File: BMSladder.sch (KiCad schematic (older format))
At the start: 30 parts, among them J1 Solder in Crimp, J2 Solder in Crimp, J3 HY2.0 Male, J4 Pad TH 1mm, J5 UPDI Port, J6 HY2.0 Male, J7 Solder in Crimp, Q1 MMDT3946, Q2 SI3402-TP, Q3 MMBT3904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

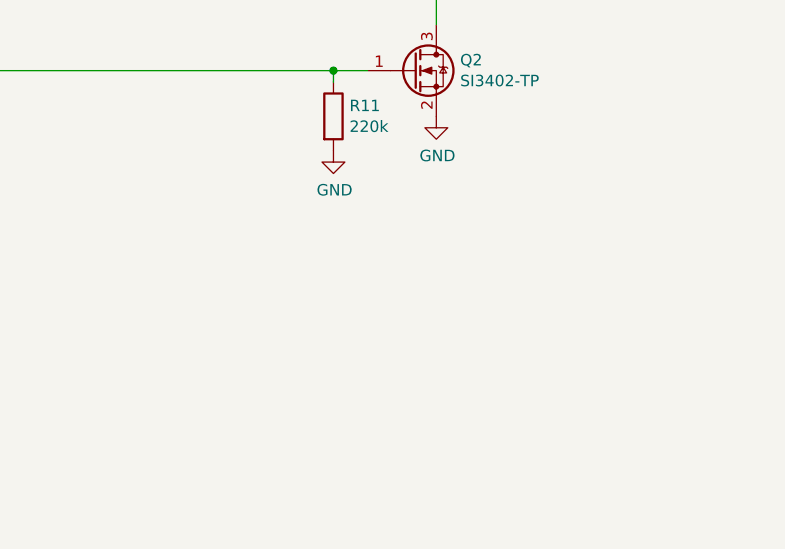
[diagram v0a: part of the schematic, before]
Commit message: Update BMSladder.sch
Added construction notes for further clarification
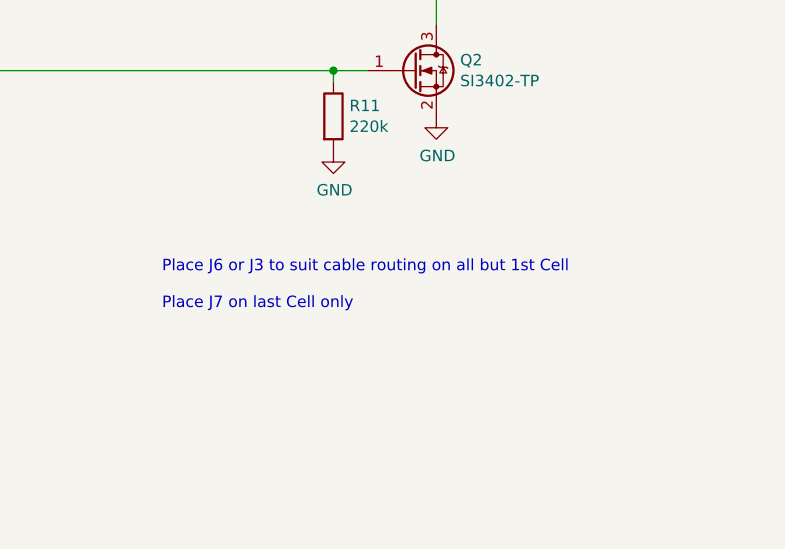
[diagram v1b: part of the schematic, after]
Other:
- note added: "Place J6 or J3 to suit cable routing on all but 1st Cell\n\nPlace J7 on last Cell only"
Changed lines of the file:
@@
 Wire Wire Line
 	5650 2800 6150 2800
+Text Notes 6900 5800 0    50   ~ 0
+Place J6 or J3 to suit cable routing on all but 1st Cell\n\nPlace J7 on last Cell only
 $EndSCHEMATC

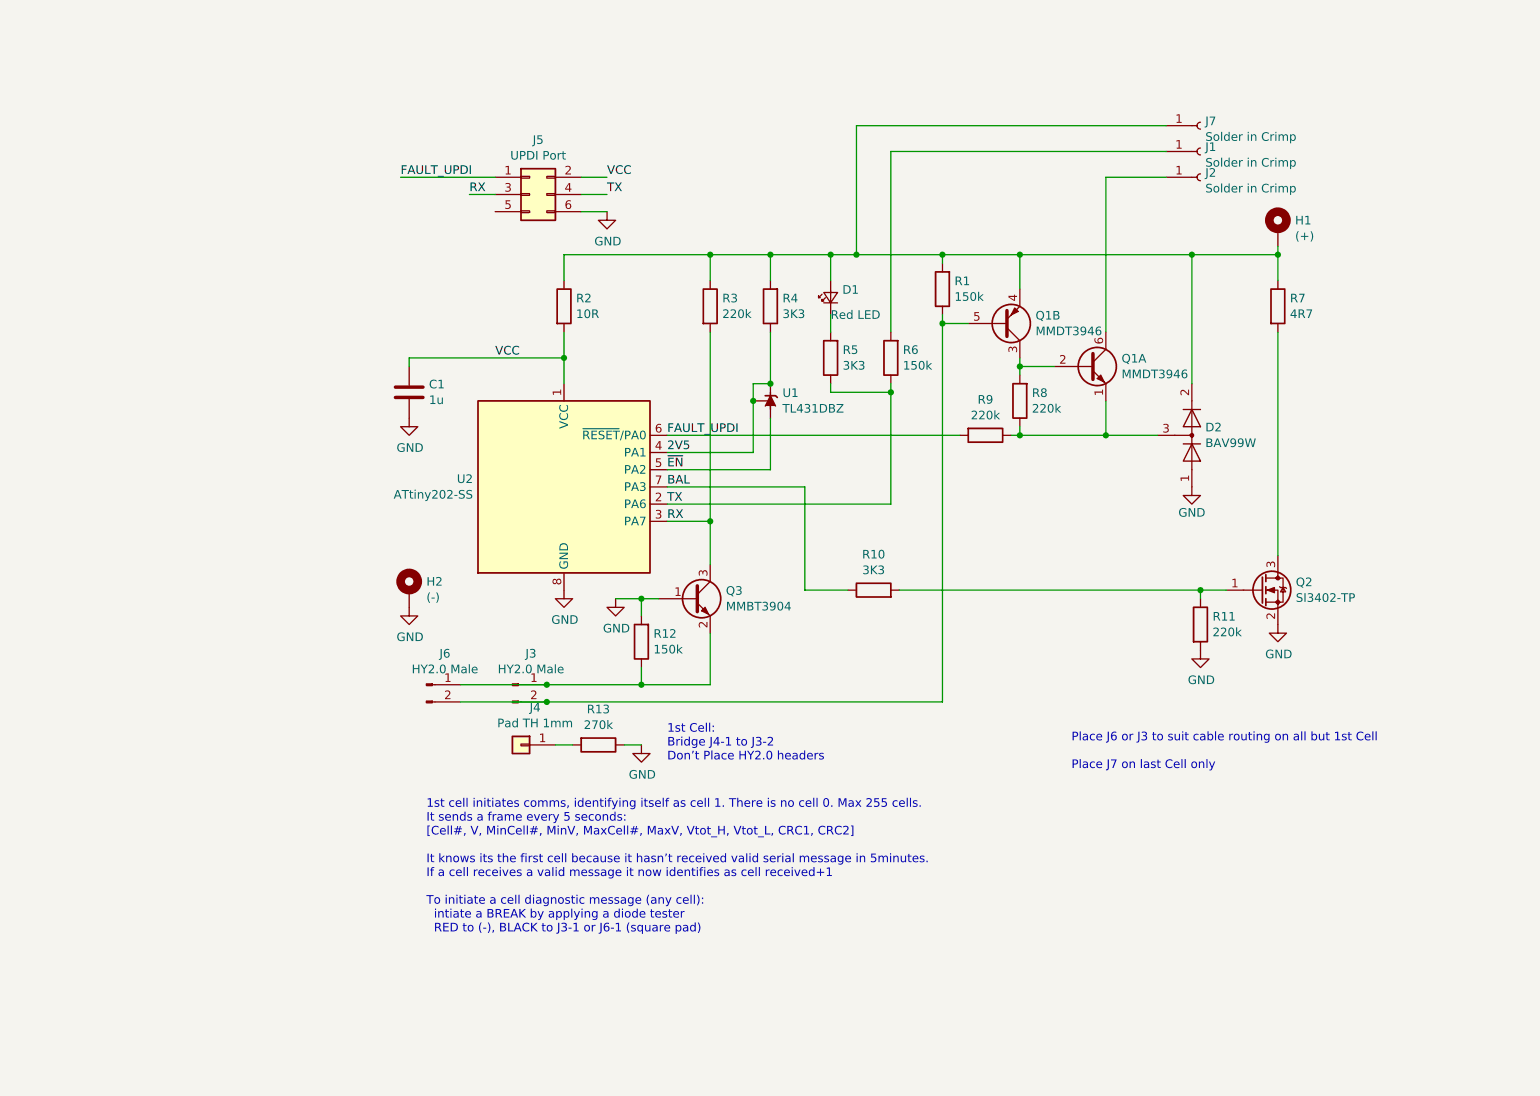
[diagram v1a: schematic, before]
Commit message: Improve connections
Most fiddly thing with v1.0 was the tail and connectors. changing to a surface mount connector (easy assembly), commonly available lead (if modified to remove one wire).
Also, uC pin swap as per Heins mod
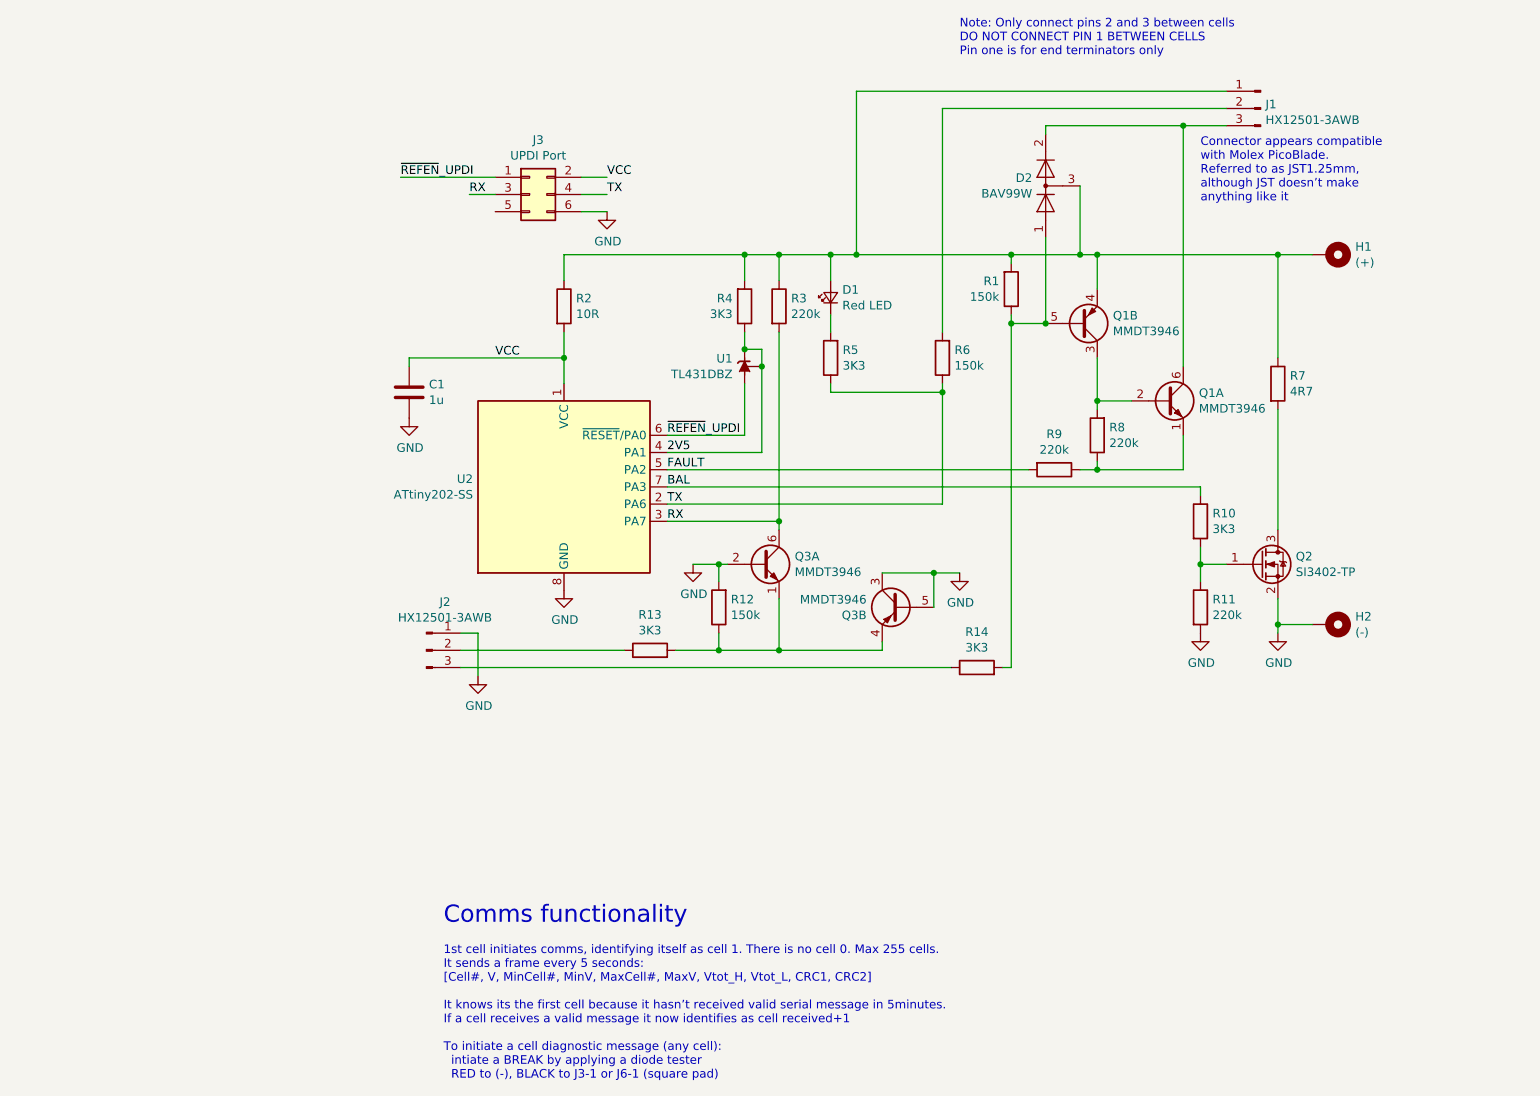
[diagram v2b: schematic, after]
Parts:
- removed J1, J2, J7: Solder in Crimp, Connector_Pin:Pin_D0.9mm_L10.0mm_W2.4mm_FlatFork, symbol Connector:Conn_01x01_Female
- removed J3, J6: HY2.0 Male, EdsKicadLibrary:HY2.0mm2P_Header_Horizontal, symbol Connector:Conn_01x02_Male
- removed J4: Pad TH 1mm, Connector_Pin:Pin_D1.0mm_L10.0mm, symbol Connector_Generic:Conn_01x01
- removed Q3: MMBT3904, Package_TO_SOT_SMD:SOT-23, symbol Transistor_BJT:MMBT3904
- added J1, J2: HX12501-3AWB, Connector_Molex:Molex_PicoBlade_53261-0371_1x03-1MP_P1.25mm_Horizontal, symbol Connector:Conn_01x03_Male
- added Q3: MMDT3946, Package_TO_SOT_SMD:SOT-363_SC-70-6, symbol Transistor_BJT:MMDT3946
- added R14: 3K3, Resistor_SMD:R_0603_1608Metric, symbol Device:R
- R13: value 270k -> 3K3
- renumbered J5 to J3
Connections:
- net GND: now also J2.1 (Pin_1), Q3.2 (B1), Q3.3 (C2), Q3.5 (B2); no longer D2.1 (K), R13.1
- net RX: now also Q3.6 (C1)
- net at R12.1: now also R13.2, Q3.1 (E1), Q3.4 (E2)
- net at Q1.1 (E1), R8.1, R9.1: no longer D2.3 (K)
- net at Q1.6 (C1): now also D2.2 (A), J1.3 (Pin_3)
- net at D1.2 (A), H1.1, Q1.4 (E2)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: now also D2.3 (K), J1.1 (Pin_1); no longer D2.2 (A)
- net at Q1.5 (B2), R1.1: now also D2.1 (K), R14.2
- net at R6.2: now also J1.2 (Pin_2)
- net FAULT_UPDI renamed ~REFEN~_UPDI
- net ~REFEN~_UPDI: now also U1.3 (A); no longer R9.2
- net ~EN renamed FAULT
- net FAULT: now also R9.2; no longer U1.3 (A)
- new net: J2.2 (Pin_2), R13.1
- new net: J2.3 (Pin_3), R14.1
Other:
- note added: "Comms functionality"
- note added: "Connector appears compatible\nwith Molex PicoBlade.\nReferred to as JST1.25mm,\nalthough JST doesn’t make\nanything like it"
- note added: "Note: Only connect pins 2 and 3 between cells\nDO NOT CONNECT PIN 1 BETWEEN CELLS\nPin one is for end terminators only"
- note removed: "1st Cell:\nBridge J4-1 to J3-2\nDon’t Place HY2.0 headers"
- note removed: "Place J6 or J3 to suit cable routing on all but 1st Cell\n\nPlace J7 on last Cell only"
- moved on the sheet: D2, H1, H2, Q1A, Q1B, Q2, R1, R10, R11, R12, R3, R4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

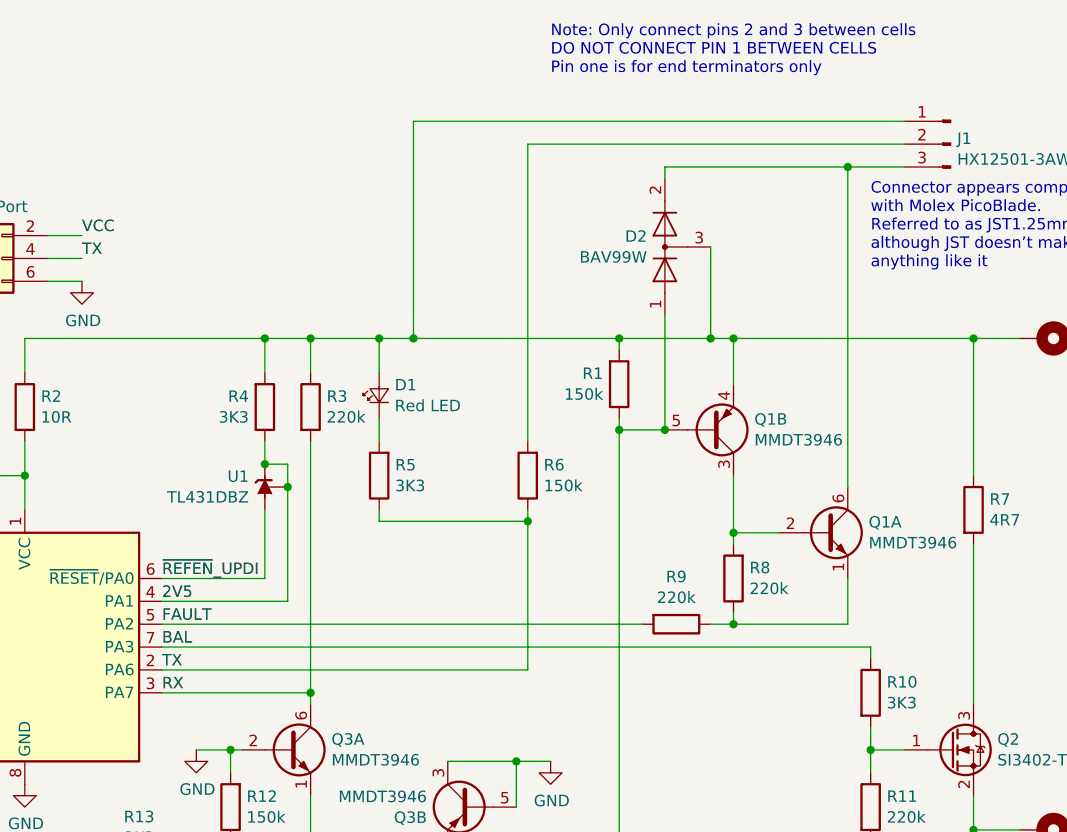
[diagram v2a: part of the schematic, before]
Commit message: old changes kept just in case
not sure why
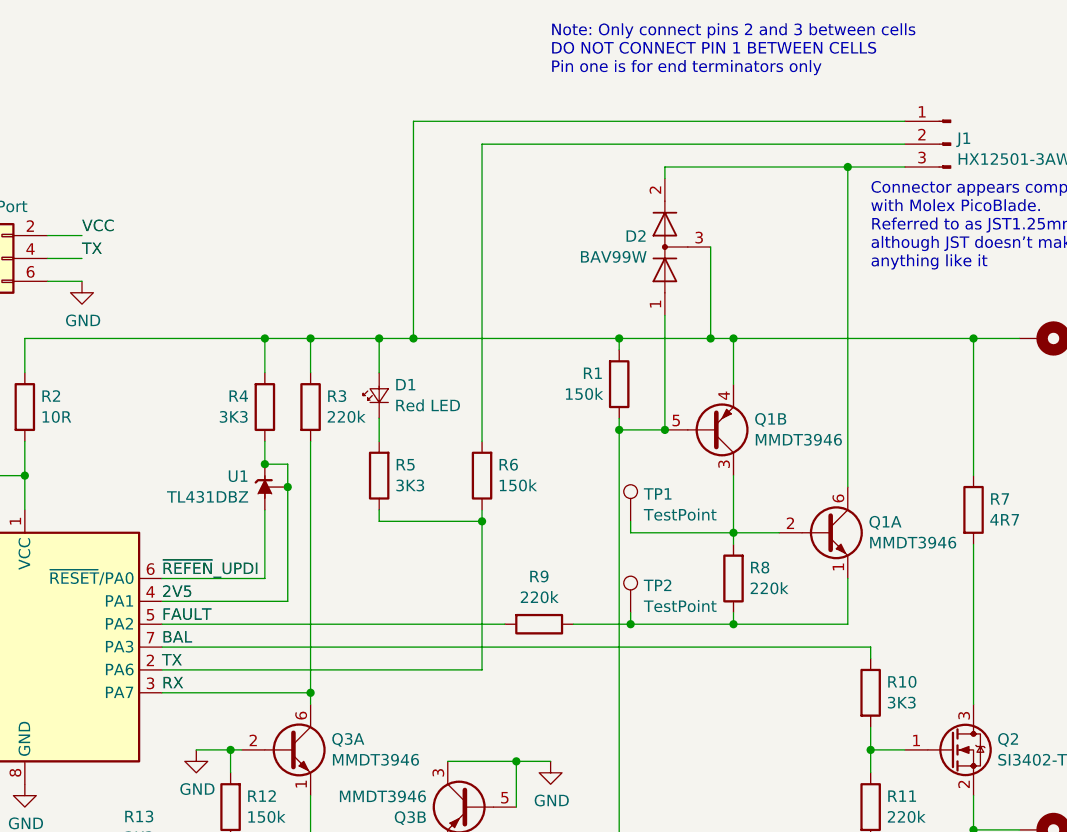
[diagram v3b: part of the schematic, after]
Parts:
- added TP1, TP2: TestPoint, TestPoint:TestPoint_Pad_D2.0mm, symbol Connector:TestPoint
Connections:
- net at Q1.1 (E1), R8.1, R9.1: now also TP2.1
- net at Q1.2 (B1), Q1.3 (C2), R8.2: now also TP1.1
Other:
- moved on the sheet: R6, R9
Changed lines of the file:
@@
 	3950 3250 3950 3400
 Wire Wire Line
-	6150 3250 6150 1950
+	5950 3250 5950 1950
 Wire Wire Line
 	5200 3250 5200 4350
@@
 	5500 3550 5500 3600
 Wire Wire Line
-	5500 3600 6150 3600
-Wire Wire Line
-	6150 3600 6150 3550
+	5500 3600 5950 3600
+Wire Wire Line
+	5950 3600 5950 3550
 Wire Wire Line
 	7050 4000 7050 4050
@@
 L Device:R R9
 U 1 1 619AAA79
-P 6800 4050
-F 0 "R9" V 6593 4050 50  0000 C CNN
-F 1 "220k" V 6684 4050 50  0000 C CNN
-F 2 "Resistor_SMD:R_0603_1608Metric" V 6730 4050 50  0001 C CNN
-F 3 "~" H 6800 4050 50  0001 C CNN
-	1    6800 4050
+P 6200 4050
+F 0 "R9" V 5993 4050 50  0000 C CNN
+F 1 "220k" V 6084 4050 50  0000 C CNN
+F 2 "Resistor_SMD:R_0603_1608Metric" V 6130 4050 50  0001 C CNN
+F 3 "~" H 6200 4050 50  0001 C CNN
+	1    6200 4050
 	0    1    1    0
 $EndComp
@@
 L Device:R R6
 U 1 1 619AB3DF
-P 6150 3400
-F 0 "R6" H 6080 3354 50  0000 R CNN
-F 1 "150k" H 6080 3445 50  0000 R CNN
-F 2 "Resistor_SMD:R_0603_1608Metric" V 6080 3400 50  0001 C CNN
-F 3 "~" H 6150 3400 50  0001 C CNN
-	1    6150 3400
+P 5950 3400
+F 0 "R6" H 5880 3354 50  0000 R CNN
+F 1 "150k" H 5880 3445 50  0000 R CNN
+F 2 "Resistor_SMD:R_0603_1608Metric" V 5880 3400 50  0001 C CNN
+F 3 "~" H 5950 3400 50  0001 C CNN
+	1    5950 3400
 	-1   0    0    1
 $EndComp
@@
 Connection ~ 8100 2800
 Wire Wire Line
-	6150 1950 7800 1950
+	5950 1950 7800 1950
 Wire Wire Line
 	7550 2050 7800 2050
@@
 Connection ~ 5000 2800
 Wire Wire Line
-	6150 4250 6150 3600
-Wire Wire Line
-	4550 4250 6150 4250
-Connection ~ 6150 3600
+	5950 4250 5950 3600
+Wire Wire Line
+	4550 4250 5950 4250
+Connection ~ 5950 3600
 Wire Wire Line
 	5500 2950 5500 2800
@@
 	5000 3850 4550 3850
 Wire Wire Line
-	6650 4050 4550 4050
-Wire Wire Line
-	7050 4050 6950 4050
+	6050 4050 4550 4050
+Wire Wire Line
+	7050 4050 6600 4050
 Connection ~ 7050 4050
 $Comp
@@
 Text Notes 7650 2500 0    50   ~ 0
 Connector appears compatible\nwith Molex PicoBlade.\nReferred to as JST1.25mm,\nalthough JST doesn’t make\nanything like it
+$Comp
+L Connector:TestPoint TP1
+U 1 1 6393EAFB
+P 6600 3600
+F 0 "TP1" H 6658 3718 50  0000 L CNN
+F 1 "TestPoint" H 6658 3627 50  0000 L CNN
+F 2 "TestPoint:TestPoint_Pad_D2.0mm" H 6800 3600 50  0001 C CNN
+F 3 "~" H 6800 3600 50  0001 C CNN
+	1    6600 3600
+	1    0    0    -1
+$EndComp
+$Comp
+L Connector:TestPoint TP2
+U 1 1 6393F51C
+P 6600 4000
+F 0 "TP2" H 6658 4118 50  0000 L CNN
+F 1 "TestPoint" H 6658 4027 50  0000 L CNN
+F 2 "TestPoint:TestPoint_Pad_D2.0mm" H 6800 4000 50  0001 C CNN
+F 3 "~" H 6800 4000 50  0001 C CNN
+	1    6600 4000
+	1    0    0    -1
+$EndComp
+Wire Wire Line
+	6600 3650 7050 3650
+Wire Wire Line
+	6600 4000 6600 4050
+Connection ~ 6600 4050
+Wire Wire Line
+	6600 4050 6350 4050
+Wire Wire Line
+	6600 3600 6600 3650
 $EndSCHEMATC
